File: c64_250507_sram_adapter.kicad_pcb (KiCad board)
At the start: 2 copper layers, 53.3 x 59.7 mm, 19 parts, among them J1 TL_DRAM, J10 B_03, J2 TR_DRAM, J3 BL_DRAM, J4 BR_DRAM, J5 T_01, J6 T_02, J7 T_03, J8 B_01, J9 B_02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

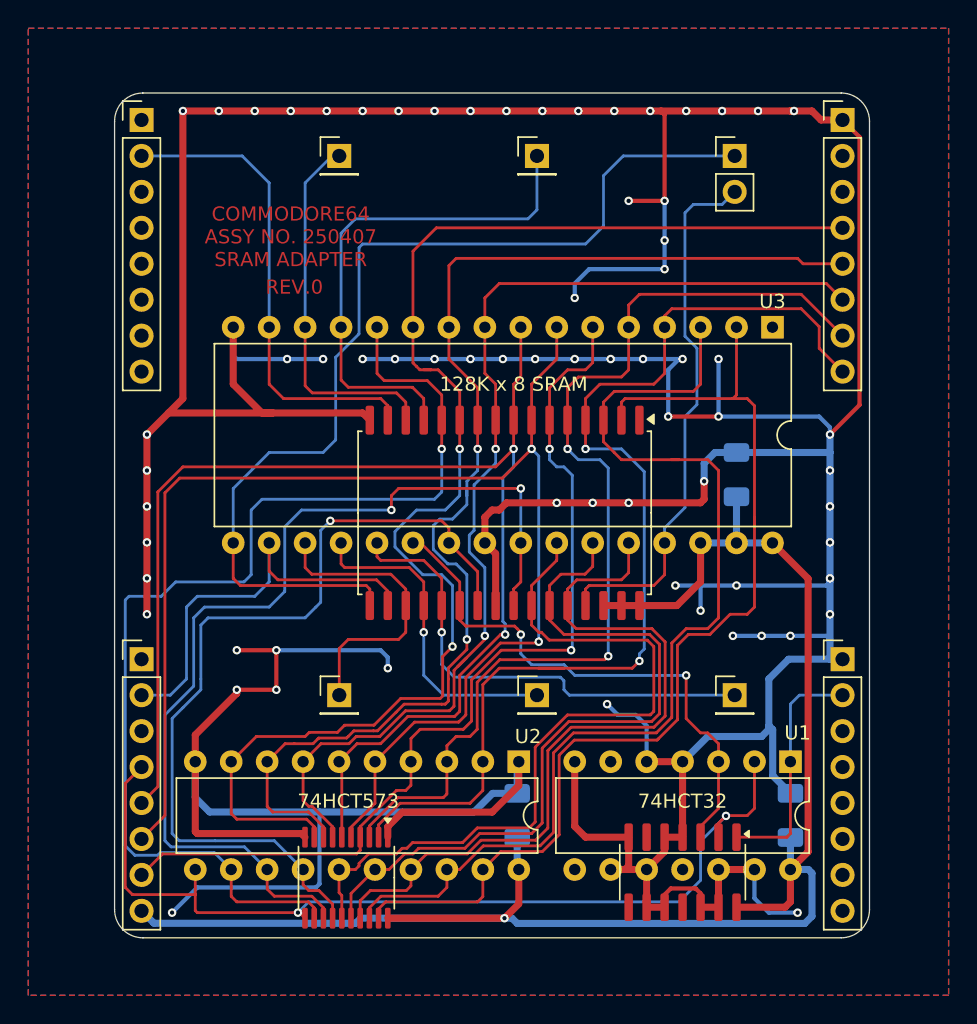
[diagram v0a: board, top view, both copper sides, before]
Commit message: Rev. 1 with better power trace
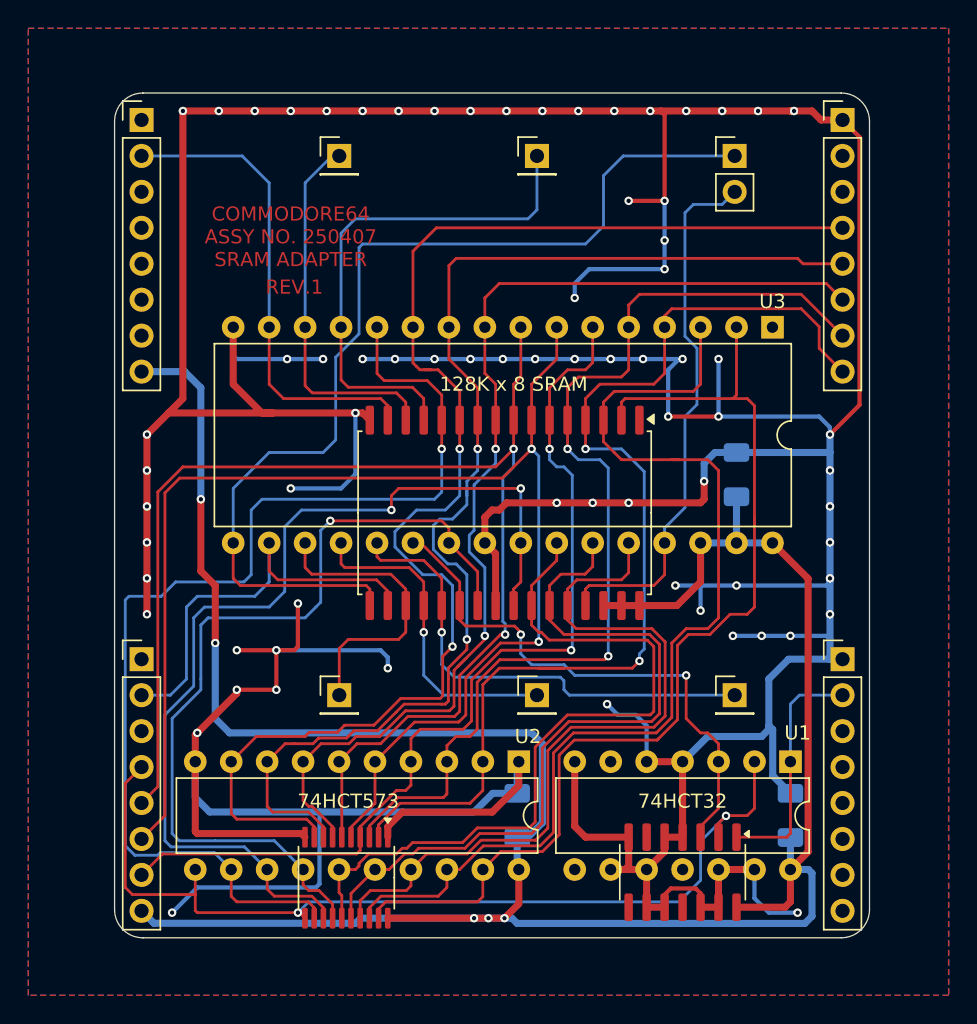
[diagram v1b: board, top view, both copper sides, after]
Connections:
- J1 pad 8: unconnected-(J1-Pin_8-Pad8) -> VCC
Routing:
- net VCC: track 119.7 -> 179.8 mm, vias 1 -> 5
- net GND: track 440.9 -> 454.9 mm, vias 68 -> 72
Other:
- board text added: "REV.1"
- board text removed: "REV.0"

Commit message: Further tweak rev.1
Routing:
- net /A7: track 74.4 -> 73.7 mm
- net /MA6: track 98.5 -> 97.8 mm
- net /A2: track 53.9 -> 53.4 mm
- net GND: vias 72 -> 73
